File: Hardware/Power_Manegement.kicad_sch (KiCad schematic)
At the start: 74 parts, among them IC1 BQ51003YFPR, IC2 CSD75207W15, IC3 BQ25185DLHR, IC4 BQ27427YZFR, IC5 BD8316GWL-E2, IC6 TLV62585DRLR, IC7 TPS7A3901DSCR, J1 Conn_01x03, J10 Conn_01x03, J11 Conn_01x03, J2 Conn_01x02, J3 Conn_01x03, J4 Conn_01x02, J5 Conn_01x02, J6 Conn_01x02, J7 Conn_01x02, J8 Conn_01x02, J9 S2B-PH-SM4-TB, U12 USB4105

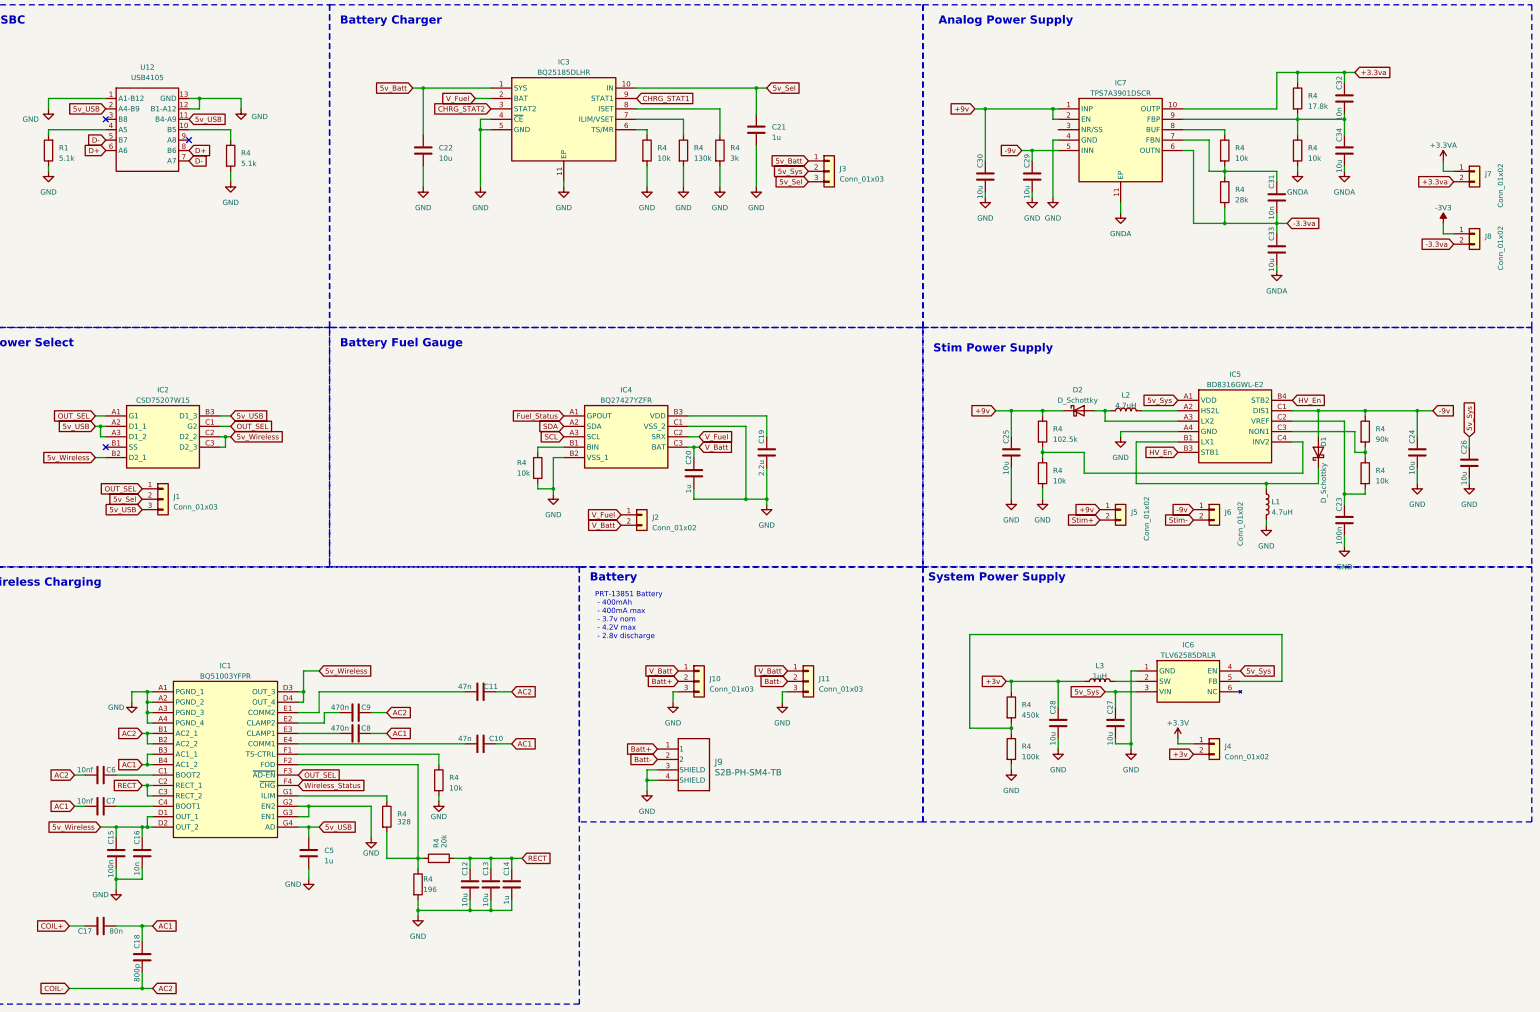
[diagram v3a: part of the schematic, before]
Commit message: Spec all components
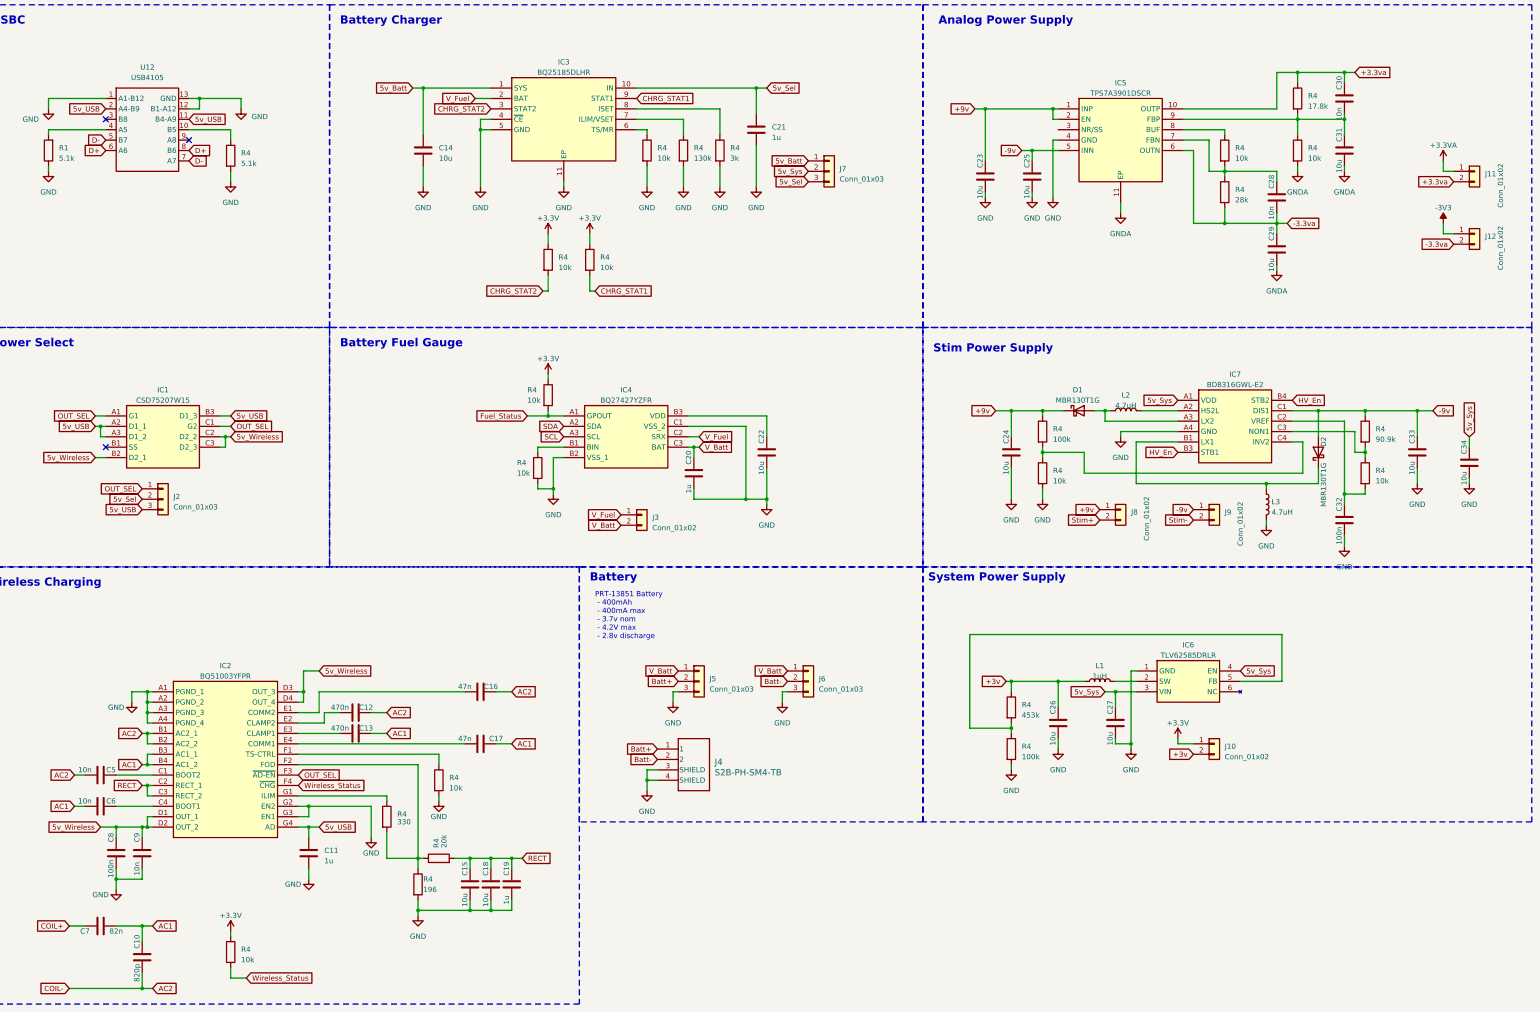
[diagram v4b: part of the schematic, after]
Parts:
- added R4 (x4): 10k, Resistor_SMD:R_0402_1005Metric, symbol Device:R
- C10: renamed from C18; value 800p -> 820p; footprint (none) -> Capacitor_SMD:C_0402_1005Metric
- C11: renamed from C5; footprint (none) -> Capacitor_SMD:C_0603_1608Metric
- C12: renamed from C9; footprint (none) -> Capacitor_SMD:C_0603_1608Metric
- C13: renamed from C8; footprint (none) -> Capacitor_SMD:C_0603_1608Metric
- C14: renamed from C22; footprint (none) -> Capacitor_SMD:C_0805_2012Metric
- C15: renamed from C12; footprint (none) -> Capacitor_SMD:C_0805_2012Metric
- C16: renamed from C11; footprint (none) -> Capacitor_SMD:C_0402_1005Metric
- C17: renamed from C10; footprint (none) -> Capacitor_SMD:C_0402_1005Metric
- C18: renamed from C13; footprint (none) -> Capacitor_SMD:C_0805_2012Metric
- C19: renamed from C14; footprint (none) -> Capacitor_SMD:C_0603_1608Metric
- C20, C21: footprint (none) -> Capacitor_SMD:C_0603_1608Metric
- C22: renamed from C19; value 2.2u -> 10u; footprint (none) -> Capacitor_SMD:C_0805_2012Metric
- C23: renamed from C30; footprint (none) -> Capacitor_SMD:C_0805_2012Metric
- C24: renamed from C25; footprint (none) -> Capacitor_SMD:C_0805_2012Metric
- C25: renamed from C29; footprint (none) -> Capacitor_SMD:C_0805_2012Metric
- C26: renamed from C28; footprint (none) -> Capacitor_SMD:C_0805_2012Metric
- C27: footprint (none) -> Capacitor_SMD:C_0805_2012Metric
- C28: renamed from C31; footprint (none) -> Capacitor_SMD:C_0402_1005Metric
- C29: renamed from C33; footprint (none) -> Capacitor_SMD:C_0805_2012Metric
- C30: renamed from C32; footprint (none) -> Capacitor_SMD:C_0402_1005Metric
- C31: renamed from C34; footprint (none) -> Capacitor_SMD:C_0805_2012Metric
- C32: renamed from C23; footprint (none) -> Capacitor_SMD:C_0402_1005Metric
- C33: renamed from C24; footprint (none) -> Capacitor_SMD:C_0805_2012Metric
- C34: renamed from C26; footprint (none) -> Capacitor_SMD:C_0805_2012Metric
- C5: renamed from C6; value 10nf -> 10n; footprint (none) -> Capacitor_SMD:C_0402_1005Metric
- C6: renamed from C7; value 10nf -> 10n; footprint (none) -> Capacitor_SMD:C_0402_1005Metric
- C7: renamed from C17; value 80n -> 82n; footprint (none) -> Capacitor_SMD:C_1206_3216Metric
- C8: renamed from C15; footprint (none) -> Capacitor_SMD:C_0402_1005Metric
- C9: renamed from C16; footprint (none) -> Capacitor_SMD:C_0402_1005Metric
- D1: renamed from D2; value D_Schottky -> MBR130T1G; footprint (none) -> Diode_SMD:D_SOD-123
- D2: renamed from D1; value D_Schottky -> MBR130T1G; footprint (none) -> Diode_SMD:D_SOD-123
- J10: renamed from J4; footprint (none) -> Connector_PinHeader_2.54mm:PinHeader_1x02_P2.54mm_Vertical
- J11: renamed from J7; footprint (none) -> Connector_PinHeader_2.54mm:PinHeader_1x02_P2.54mm_Vertical
- J12: renamed from J8; footprint (none) -> Connector_PinHeader_2.54mm:PinHeader_1x02_P2.54mm_Vertical
- J2: renamed from J1; footprint (none) -> Connector_PinHeader_2.54mm:PinHeader_1x03_P2.54mm_Vertical
- J3: renamed from J2; footprint (none) -> Connector_PinHeader_2.54mm:PinHeader_1x02_P2.54mm_Vertical
- J5: renamed from J10; footprint (none) -> Connector_PinHeader_2.54mm:PinHeader_1x03_P2.54mm_Vertical
- J6: renamed from J11; footprint (none) -> Connector_PinHeader_2.54mm:PinHeader_1x03_P2.54mm_Vertical
- J7: renamed from J3; footprint (none) -> Connector_PinHeader_2.54mm:PinHeader_1x03_P2.54mm_Vertical
- J8: renamed from J5; footprint (none) -> Connector_PinHeader_2.54mm:PinHeader_1x02_P2.54mm_Vertical
- J9: renamed from J6; footprint (none) -> Connector_PinHeader_2.54mm:PinHeader_1x02_P2.54mm_Vertical
- L1: renamed from L3; footprint (none) -> Inductor_SMD:L_Coilcraft_XAL4020-XXX
- L2: footprint (none) -> Inductor_SMD:L_0603_1608Metric
- L3: renamed from L1; footprint (none) -> Inductor_SMD:L_0603_1608Metric
- R1, R4: footprint (none) -> Resistor_SMD:R_0402_1005Metric
- R4: value 102.5k -> 100k; footprint (none) -> Resistor_SMD:R_0402_1005Metric
- R4: value 328 -> 330; footprint (none) -> Resistor_SMD:R_0402_1005Metric
- R4: value 90k -> 90.9k; footprint (none) -> Resistor_SMD:R_0402_1005Metric
- R4: value 450k -> 453k; footprint (none) -> Resistor_SMD:R_0402_1005Metric
- renumbered IC2 to IC1, IC1 to IC2, IC7 to IC5, IC5 to IC7, J9 to J4
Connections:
- net +3.3V: now also R4.1, R4.1, R4.1, R4.1
- net CHRG_STAT1: now also R4.2
- net CHRG_STAT2: now also R4.2
- net Fuel_Status: now also R4.2
- net Wireless_Status: now also R4.2

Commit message: Start Layout
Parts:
- removed C17: 47n, Capacitor_SMD:C_0402_1005Metric, symbol Device:C
- removed C18: 10u, Capacitor_SMD:C_0805_2012Metric, symbol Device:C
- removed C19: 1u, Capacitor_SMD:C_0603_1608Metric, symbol Device:C
- removed IC1: CSD75207W15, BQ51003YFPR:BGA9C50P3X3_146X146X62, symbol CSD75207W15:CSD75207W15
- removed IC2: BQ51003YFPR, BQ51003YFPR:BGA28C40P4X7_188X301X50, symbol BQ51003YFPR:BQ51003YFPR
- removed IC3: BQ25185DLHR, BQ51003YFPR:SON40P220X200X80-11N, symbol BQ25185DLHR:BQ25185DLHR
- removed IC4: BQ27427YZFR, BQ51003YFPR:BGA9C50P3X3_158X162X62, symbol BQ27427YZFR:BQ27427YZFR
- removed IC5: TPS7A3901DSCR, BQ51003YFPR:SON50P300X300X80-11N-D, symbol TPS7A3901DSCR:TPS7A3901DSCR
- removed IC6: TLV62585DRLR, BQ51003YFPR:SOTFL50P160X60-6N, symbol TLV62585DRLR:TLV62585DRLR
- removed IC7: BD8316GWL-E2, BQ51003YFPR:BGA11C40P4X3_180X150X55, symbol BD8316GWL-E2:BD8316GWL-E2
- removed J4: S2B-PH-SM4-TB, BQ51003YFPR:CONN_S2B-PH-SM4-TB_JST, symbol 2024-03-26_04-39-57:S2B-PH-SM4-TB
- removed R4: 20k, Resistor_SMD:R_0402_1005Metric, symbol Device:R
- removed R4: 10k, Resistor_SMD:R_0402_1005Metric, symbol Device:R
- removed R4: 196, Resistor_SMD:R_0402_1005Metric, symbol Device:R
- removed R4: 330, Resistor_SMD:R_0402_1005Metric, symbol Device:R
- added C10: 1u, Capacitor_SMD:C_0603_1608Metric, symbol Device:C
- added C14: 10u, Capacitor_SMD:C_0805_2012Metric, symbol Device:C
- added C7: 470n, Capacitor_SMD:C_0603_1608Metric, symbol Device:C
- added IC1: BQ51013BRHLR, Neural_Footprints:BQ51050BRHLR, symbol Neural_Components:BQ51013BRHLR
- added IC2: CSD75207W15, Neural_Footprints:BGA9C50P3X3_146X146X62, symbol Neural_Components:CSD75207W15
- added IC3: BQ25185DLHR, Neural_Footprints:SON40P220X200X80-11N, symbol Neural_Components:BQ25185DLHR
- added IC4: BQ27427YZFR, Neural_Footprints:BGA9C50P3X3_158X162X62, symbol Neural_Components:BQ27427YZFR
- added IC5: TPS7A3901DSCR, Neural_Footprints:SON50P300X300X80-11N-D, symbol Neural_Components:TPS7A3901DSCR
- added IC6: TLV62585DRLR, Neural_Footprints:SOTFL50P160X60-6N, symbol Neural_Components:TLV62585DRLR
- added IC7: BD8316GWL-E2, Neural_Footprints:BGA11C40P4X3_180X150X55, symbol Neural_Components:BD8316GWL-E2
- added J7: S2B-PH-SM4-TB, Neural_Footprints:CONN_S2B-PH-SM4-TB_JST, symbol Neural_Components:S2B-PH-SM4-TB
- added R4: 196, Resistor_SMD:R_0402_1005Metric, symbol Device:R
- added R4: 20k, Resistor_SMD:R_0402_1005Metric, symbol Device:R
- added R4: 330, Resistor_SMD:R_0402_1005Metric, symbol Device:R
- added R4: 10k, Resistor_SMD:R_0402_1005Metric, symbol Device:R
- added TP1, TP4: TestPoint, TestPoint:TestPoint_Pad_1.0x1.0mm, symbol Connector:TestPoint
- added TP2, TP3: TestPoint, TestPoint:TestPoint_Pad_4.0x4.0mm, symbol Connector:TestPoint
- C11: value 1u -> 47n; footprint Capacitor_SMD:C_0603_1608Metric -> Capacitor_SMD:C_0402_1005Metric
- C13: value 470n -> 10n; footprint Capacitor_SMD:C_0603_1608Metric -> Capacitor_SMD:C_0402_1005Metric
- C16: value 47n -> 1u; footprint Capacitor_SMD:C_0402_1005Metric -> Capacitor_SMD:C_0603_1608Metric
- C5: value 10n -> 100n
- C8: value 100n -> 47n
- J8: renamed from J5; footprint Connector_PinHeader_2.54mm:PinHeader_1x03_P2.54mm_Vertical -> Jumper:SolderJumper-3_P1.3mm_Open_Pad1.0x1.5mm
- J9: renamed from J6; footprint Connector_PinHeader_2.54mm:PinHeader_1x03_P2.54mm_Vertical -> Jumper:SolderJumper-3_P1.3mm_Open_Pad1.0x1.5mm
- renumbered C7 to C17, C10 to C18, C14 to C19, C32 to C31, C31 to C32, J7 to J10, J8 to J11, J9 to J12, J10 to J13, J11 to J14, J12 to J15, J2 to J5, J3 to J6
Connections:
- net +3.3va: now also C32.1, IC5.10 (OUTP)
- net +9v: now also IC5.1 (INP), IC5.2 (EN)
- net -3.3va: now also IC5.6 (OUTN)
- net -9v: now also IC5.5 (INN), IC7.C1 (DIS1)
- net 5v_Batt: now also IC3.1 (SYS)
- net 5v_Sel: now also IC3.10 (IN)
- net 5v_Sys: now also IC6.3 (VIN), IC6.4 (EN), IC7.A1 (VDD)
- net 5v_USB: now also C10.1, IC1.9 (AD), IC2.A2 (D1_1), IC2.A3 (D1_2), IC2.B3 (D1_3); no longer C11.1
- net 5v_Wireless: now also C5.1, C6.1, IC1.4 (OUT), IC2.B2 (D2_1), IC2.C2 (D2_2), IC2.C3 (D2_3); no longer C8.1, C9.1
- net AC1: now also C8.1, C9.2, C7.1, IC1.2 (AC1); no longer C13.1, C6.2
- net AC2: now also C11.1, C13.2, IC1.19 (AC2), TP3.1; no longer C16.1, C5.2
- net Batt+: now also J7.1
- net Batt-: now also J7.2
- net CHRG_STAT1: now also IC3.9 (STAT1)
- net CHRG_STAT2: now also IC3.3 (STAT2)
- net COIL+: now also TP2.1
- net Fuel_Status: now also IC4.A1 (GPOUT)
- net GND: now also C16.2, C5.2, C6.2, C10.2, C14.2, IC1.1 (PGND_1), IC1.10 (EN1), IC1.11 (EN2), IC1.20 (PGND_2), IC1.21 (EP), IC3.11 (EP), IC3.4 (~{CE}), IC3.5 (GND), IC4.B2 (VSS_1), IC4.C1 (VSS_2), IC5.4 (GND), IC6.1 (GND), IC7.A4 (GND), J7.3 (SHIELD), J7.4 (SHIELD), R4.2, R4.2; no longer C11.2, C8.2, C9.2
- net GNDA: now also IC5.11 (EP)
- net HV_En: now also IC7.B3 (STB1), IC7.B4 (STB2)
- net OUT_SEL: now also IC1.8 (~{AD-EN}), IC2.A1 (G1), IC2.C1 (G2)
- net RECT: now also C16.1, C14.1, IC1.18 (RECT), R4.2
- net SCL: now also IC4.A3 (SCL)
- net SDA: now also IC4.A2 (SDA)
- net V_Batt: now also IC4.C3 (BAT)
- net V_Fuel: now also IC3.2 (BAT), IC4.C2 (SRX)
- net Wireless_Status: now also IC1.7 (~{CHG})
- net at C31.1, R4.2: now also IC7.C2 (VREF)
- net at R4.1, R4.2: now also IC6.5 (FB)
- net at R4.1: now also IC3.6 (TS/MR)
- net at D2.1 (K), L3.1: now also IC7.B1 (LX1)
- net at L2.2: now also IC7.A2 (HS2L)
- net at D1.2 (A), L2.1: now also IC7.A3 (LX2)
- net at R4.1, R4.2: now also IC7.C3 (NON1)
- net at R4.1, R4.2: now also IC7.C4 (INV2)
- net at R4.1: now also IC3.7 (ILIM/VSET)
- net at R4.1: now also IC3.8 (ISET)
- net at C12.2: now also IC1.16 (CLAMP2)
- net at R4.1: now also IC4.B1 (BIN)
- net at C22.1: now also IC4.B3 (VDD)
- net at C28.1, R4.1, R4.2: now also IC5.7 (FBN)
- net at R4.1: now also IC5.8 (BUF)
- net at C30.2, R4.1, R4.2: now also IC5.9 (FBP); no longer C32.1
- net at L1.2: now also IC6.2 (SW)
- new net: IC5.3 (NR/SS), TP4.1
- new net: C8.2, IC1.6 (COMM1)
- new net: IC1.14 (FOD), R4.1, R4.1, R4.2
- new net: IC1.12 (ILIM), R4.1
- new net: IC1.13 (TS/CTRL), R4.1
- new net: C9.1, IC1.3 (BOOT1)
- new net: IC2.B1 (SS), TP1.1
- new net: C11.2, IC1.15 (COMM2)
- new net: C13.1, IC1.17 (BOOT2)
- new net: C7.2, IC1.5 (CLAMP1)
- no-connect marks 3 -> 2
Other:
- moved on the sheet: C32, J8, J9
